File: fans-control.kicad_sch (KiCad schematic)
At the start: 53 parts, among them J2 PinHeader_1x4_P2.5mm_Drill1mm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, J3 PinHeader_1x4_P2.5mm_Drill1mm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, J4 PinHeader_1x4_P2.5mm_Drill1mm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, J5 PinHeader_1x4_P2.5mm_Drill1mm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, Q4 2N7002K-T1-E3, Q5 BSS138PW, U5 LM339_TSSOP_Split, U6 TS5A3359_VSSOP, U7 74CBTLV3257_VQFN, U8 74VHC153FT

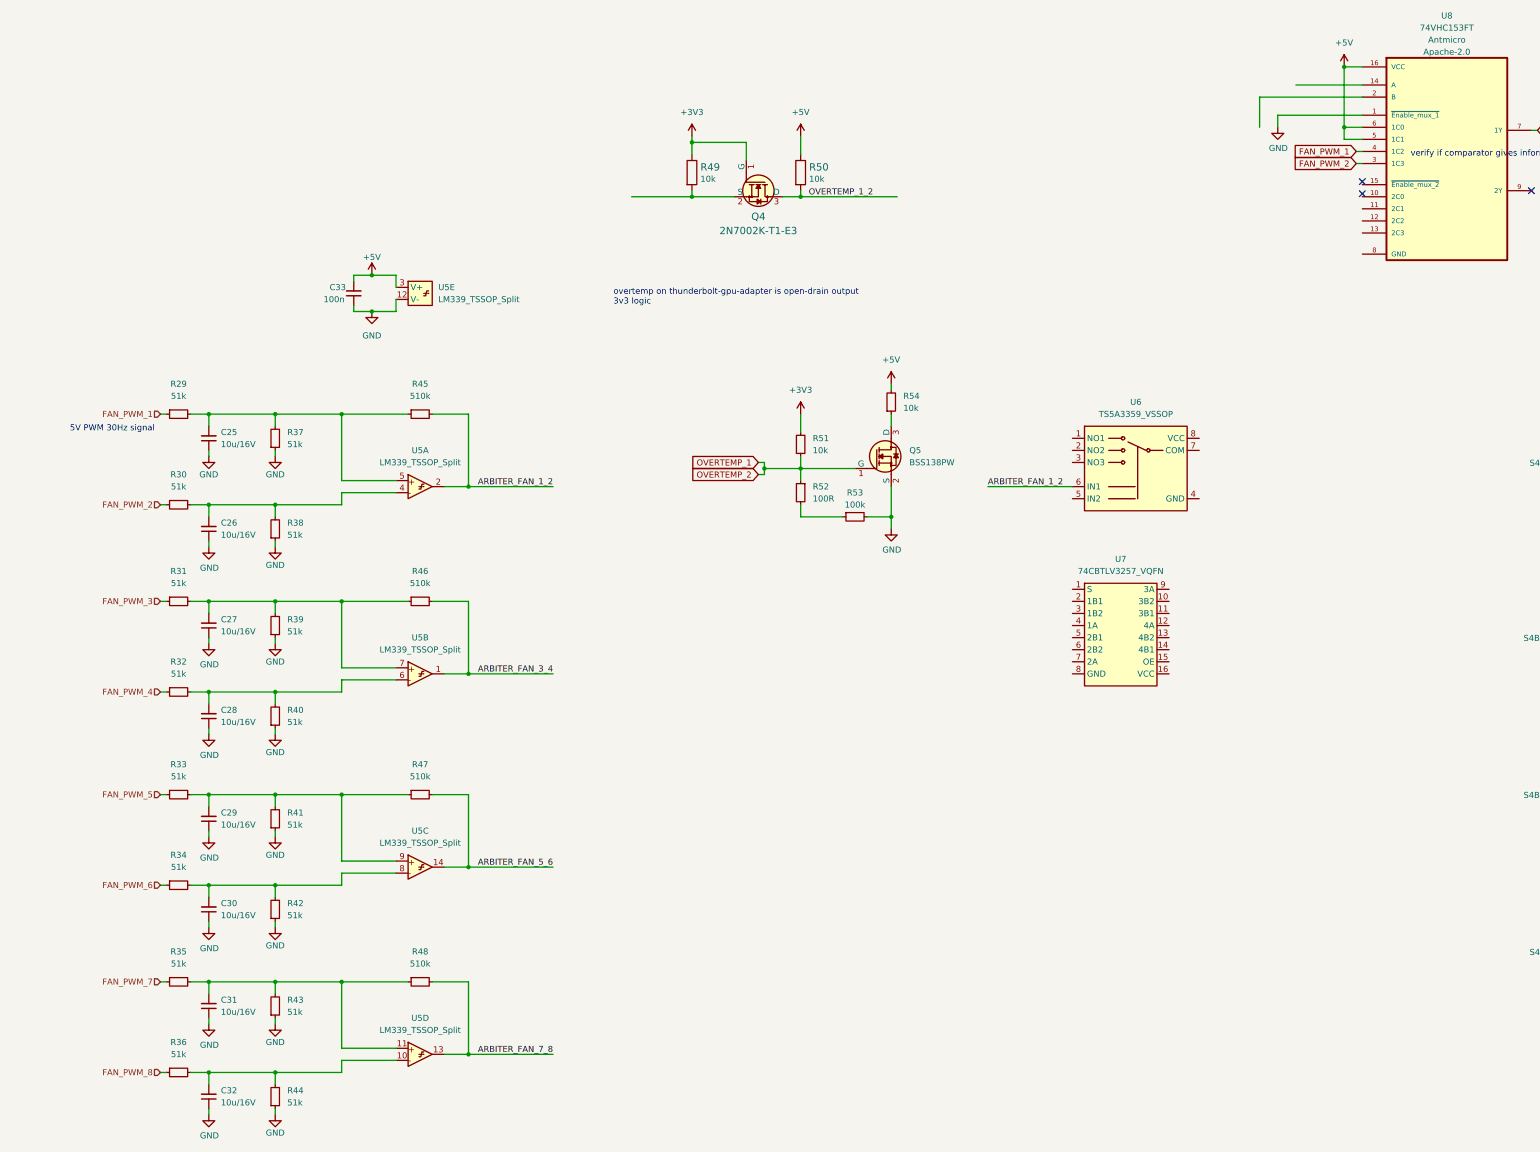
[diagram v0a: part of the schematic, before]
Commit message: Add mux for temp signals
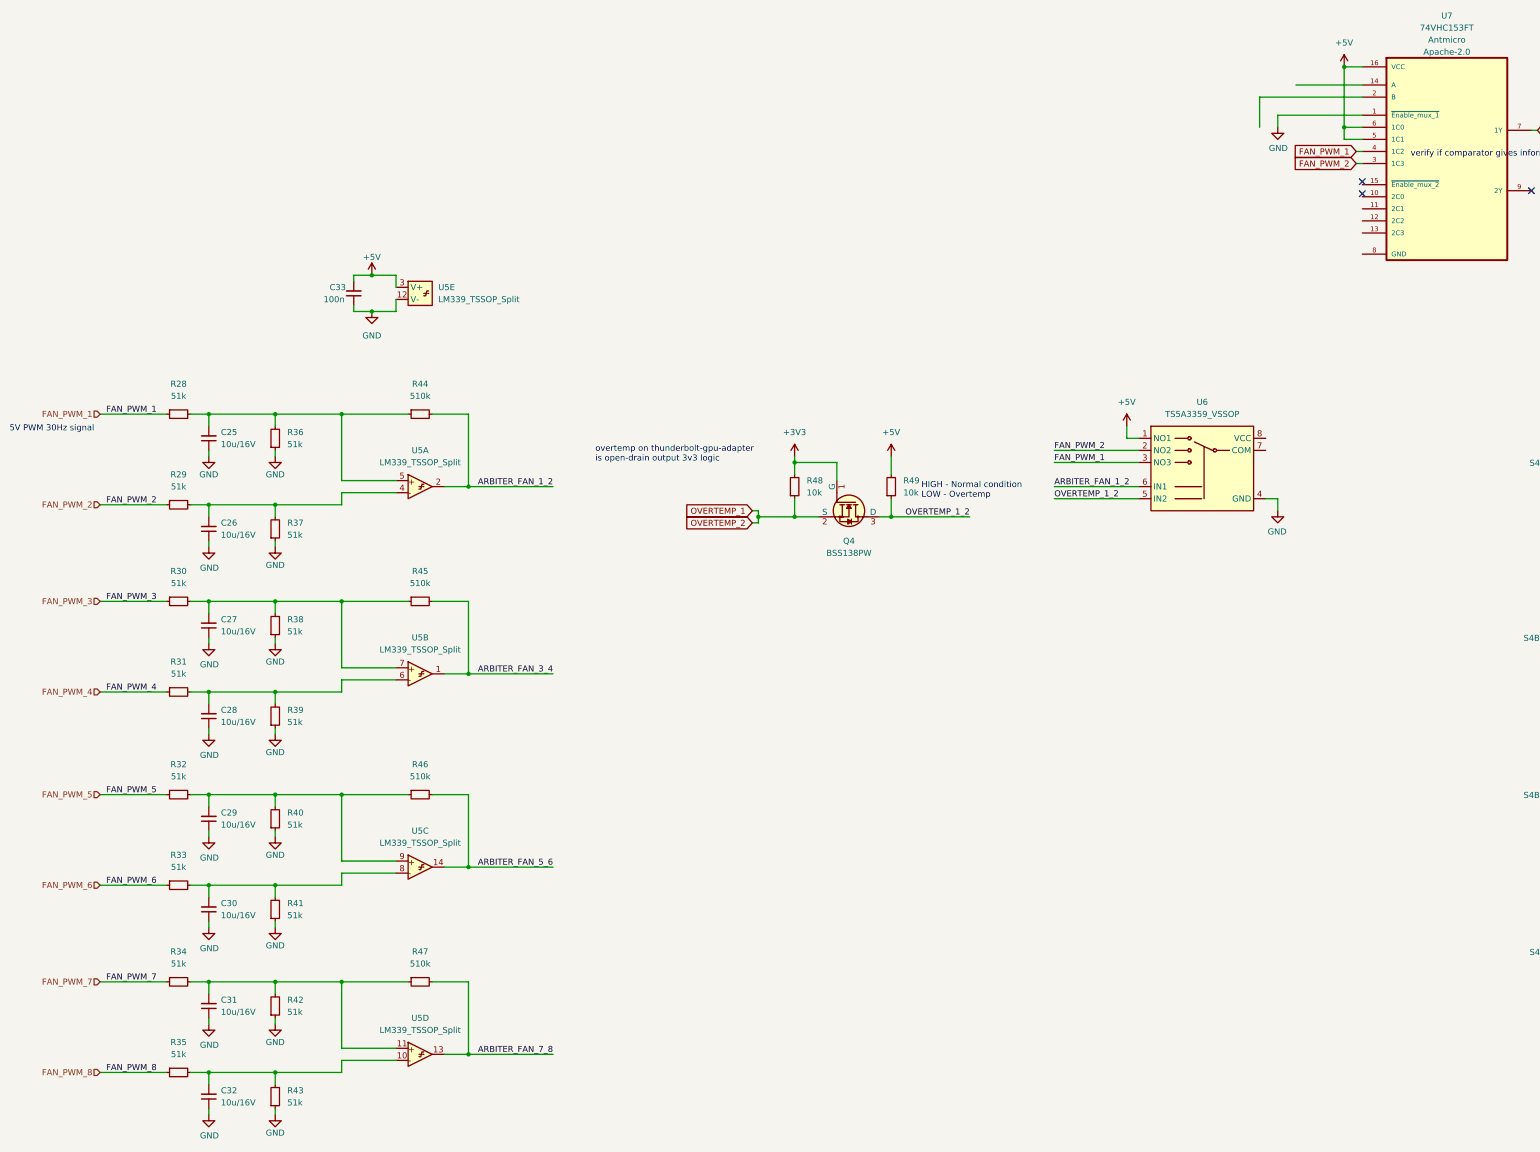
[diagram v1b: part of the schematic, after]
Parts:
- removed Q4: 2N7002K-T1-E3, antmicro-footprints:SOT-23-3, symbol antmicroTransistorsFETsMOSFETsSingle:2N7002K-T1-E3
- removed Q5: BSS138PW, antmicro-footprints:SC70-3, symbol antmicroTransistorsFETsMOSFETsSingle:BSS138PW
- removed R50, R51, R54: R_10k_0402, antmicro-footprints:R_0402_1005Metric, symbol antmicroResistors0402:R_10k_0402
- removed R52: R_100R_0402, antmicro-footprints:R_0402_1005Metric, symbol antmicroResistors0402:R_100R_0402
- removed R53: R_100k_0402, antmicro-footprints:R_0402_1005Metric, symbol antmicroResistors0402:R_100k_0402
- removed U7: 74CBTLV3257_VQFN, antmicro-footprints:DHVQFN-16-1EP_2.5x3.5mm_P0.5mm, symbol antmicroInterfaceAnalogSwitchesMultiplexersDemultiplexers:74CBTLV3257_VQFN
- added Q4: BSS138PW, antmicro-footprints:SC70-3, symbol antmicroTransistorsFETsMOSFETsSingle:BSS138PW
- added R48: R_10k_0402, antmicro-footprints:R_0402_1005Metric, symbol antmicroResistors0402:R_10k_0402
- R49: Author (none) -> Antmicro; License (none) -> Apache-2.0; MPN CRCW040210K0FKEDHP -> CR0402-FX-1002GLF; Manufacturer VISHAY -> Bourns; Tolerance (none) -> 1%
- renumbered R29 to R28, R30 to R29, R31 to R30, R32 to R31, R33 to R32, R34 to R33, R35 to R34, R36 to R35, R37 to R36, R38 to R37, R39 to R38, R40 to R39, R41 to R40, R42 to R41, R43 to R42, R44 to R43, R45 to R44, R46 to R45, R47 to R46, R48 to R47, U8 to U7
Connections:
- net +3V3: now also Q4.1 (G), R48.2; no longer R49.1
- net +5V: now also R49.2, U6.1 (NO1)
- net FAN_PWM_1: now also U6.3 (NO3)
- net FAN_PWM_2: now also U6.2 (NO2)
- net GND: now also U6.4 (GND)
- net OVERTEMP_1: now also Q4.2 (S), R48.1
- net OVERTEMP_1_2: now also R49.1, U6.5 (IN2), Q4.3 (D)
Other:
- note added: "HIGH - Normal condition LOW - Overtemp"
- moved on the sheet: U6

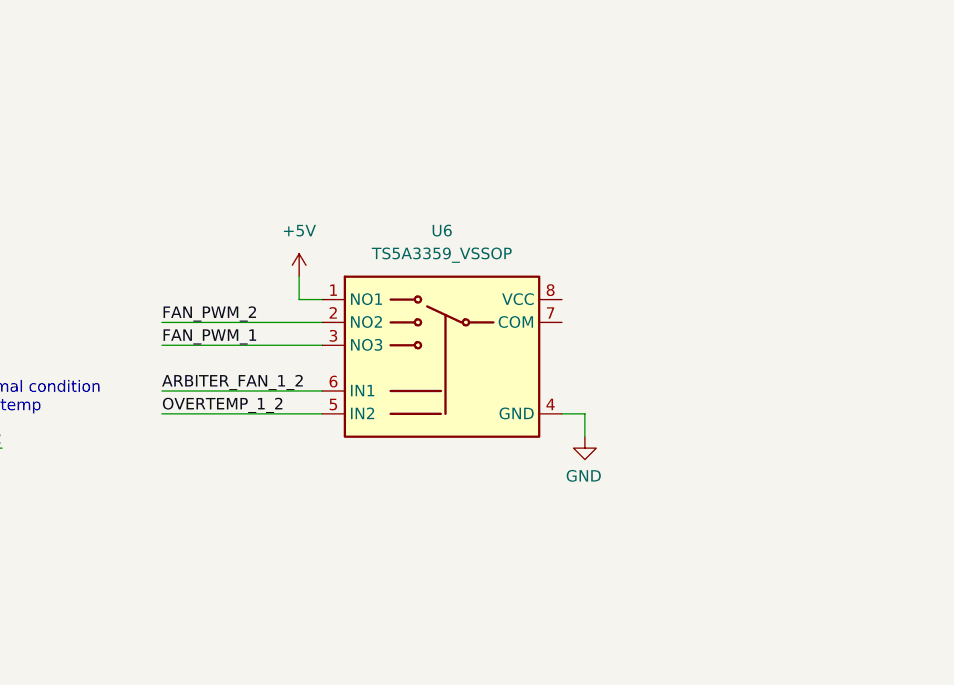
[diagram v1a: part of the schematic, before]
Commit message: Replace ft4232
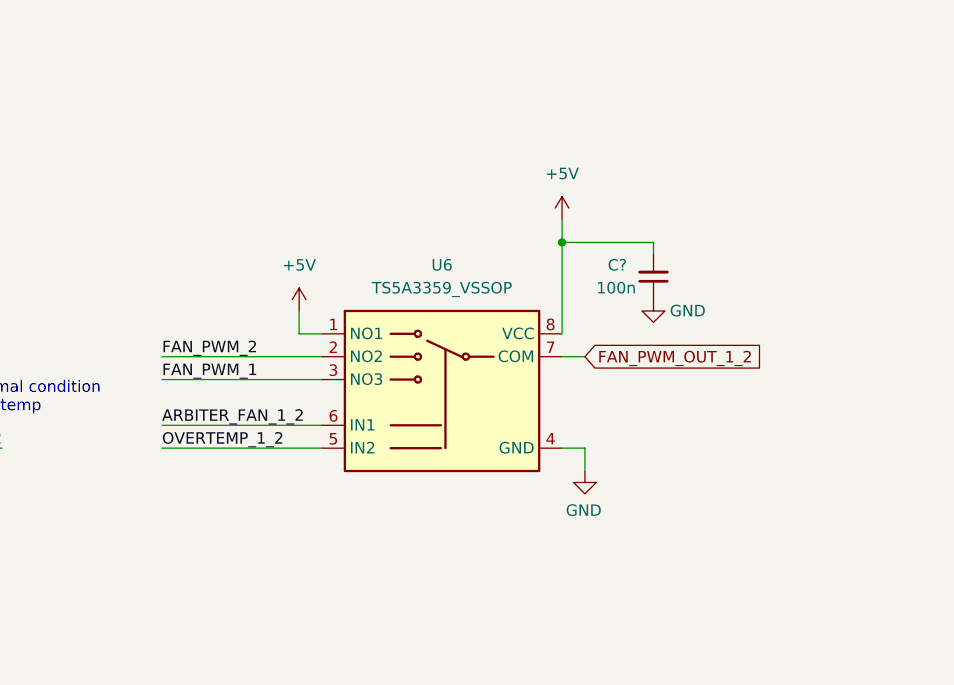
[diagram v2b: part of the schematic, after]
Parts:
- added C?: C_100n_0402, antmicro-footprints:C_0402_1005Metric, symbol antmicroCapacitors0402:C_100n_0402
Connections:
- net +5V: now also U6.8 (VCC), C?.2
- net FAN_PWM_OUT_1_2: now also U6.7 (COM)
- net GND: now also C?.1
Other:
- moved on the sheet: U6

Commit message: Reannotate
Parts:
- gave numbers to parts that had none: 1
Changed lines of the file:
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@@
   (symbol (lib_id "antmicropower:+5V") (at 294.64 -13.335 0) (unit 1)
     (in_bom yes) (on_board yes) (fields_autoplaced)
-    (property "Reference" "#PWR073" (id 0) (at 309.88 -10.795 0)
+    (property "Reference" "#PWR075" (id 0) (at 309.88 -10.795 0)
       (effects (font (size 1.27 1.27) (thickness 0.15)) (justify left bottom) hide)
     )
@@
   (symbol (lib_id "antmicropower:GND") (at 346.71 128.27 0) (unit 1)
     (in_bom yes) (on_board yes)
-    (property "Reference" "#PWR075" (id 0) (at 346.71 134.62 0)
+    (property "Reference" "#PWR077" (id 0) (at 346.71 134.62 0)
       (effects (font (size 1.27 1.27)) hide)
     )
@@
   (symbol (lib_id "antmicropower:GND") (at 288.29 64.77 0) (mirror y) (unit 1)
     (in_bom yes) (on_board yes)
-    (property "Reference" "#PWR?" (id 0) (at 288.29 71.12 0)
+    (property "Reference" "#PWR074" (id 0) (at 288.29 71.12 0)
       (effects (font (size 1.27 1.27)) hide)
     )
@@
   (symbol (lib_id "antmicropower:GND") (at 280.67 -0.635 0) (unit 1)
     (in_bom yes) (on_board yes)
-    (property "Reference" "#PWR071" (id 0) (at 280.67 5.715 0)
+    (property "Reference" "#PWR072" (id 0) (at 280.67 5.715 0)
       (effects (font (size 1.27 1.27)) hide)
     )
@@
   (symbol (lib_id "antmicropower:GND") (at 347.98 194.31 0) (unit 1)
     (in_bom yes) (on_board yes)
-    (property "Reference" "#PWR077" (id 0) (at 347.98 200.66 0)
+    (property "Reference" "#PWR079" (id 0) (at 347.98 200.66 0)
       (effects (font (size 1.27 1.27)) hide)
     )
@@
   (symbol (lib_id "antmicropower:+5V") (at 278.13 55.88 0) (mirror y) (unit 1)
     (in_bom yes) (on_board yes) (fields_autoplaced)
-    (property "Reference" "#PWR?" (id 0) (at 262.89 58.42 0)
+    (property "Reference" "#PWR071" (id 0) (at 262.89 58.42 0)
       (effects (font (size 1.27 1.27) (thickness 0.15)) (justify left bottom) hide)
     )
@@
   (symbol (lib_id "antmicroCapacitors0402:C_100n_0402") (at 288.29 64.77 90) (unit 1)
     (in_bom yes) (on_board yes)
-    (property "Reference" "C?" (id 0) (at 283.21 60.96 90)
+    (property "Reference" "C34" (id 0) (at 283.21 60.96 90)
       (effects (font (size 1.27 1.27) (thickness 0.15)) (justify right))
     )
@@
   (symbol (lib_id "antmicropower:GND") (at 347.98 91.44 0) (unit 1)
     (in_bom yes) (on_board yes)
-    (property "Reference" "#PWR076" (id 0) (at 347.98 97.79 0)
+    (property "Reference" "#PWR078" (id 0) (at 347.98 97.79 0)
       (effects (font (size 1.27 1.27)) hide)
     )
@@
   (symbol (lib_id "antmicropower:GND") (at 345.44 161.29 0) (unit 1)
     (in_bom yes) (on_board yes)
-    (property "Reference" "#PWR074" (id 0) (at 345.44 167.64 0)
+    (property "Reference" "#PWR076" (id 0) (at 345.44 167.64 0)
       (effects (font (size 1.27 1.27)) hide)
     )
@@
   (symbol (lib_id "antmicropower:GND") (at 280.67 83.82 0) (mirror y) (unit 1)
     (in_bom yes) (on_board yes)
-    (property "Reference" "#PWR072" (id 0) (at 280.67 90.17 0)
-      (effects (font (size 1.27 1.27)) hide)
-    )
+    (property "Reference" "#PWR073" (id 0) (at 280.67 90.17 0)
+      (effects (font (size 1.27 1.27)) hide)
+    )

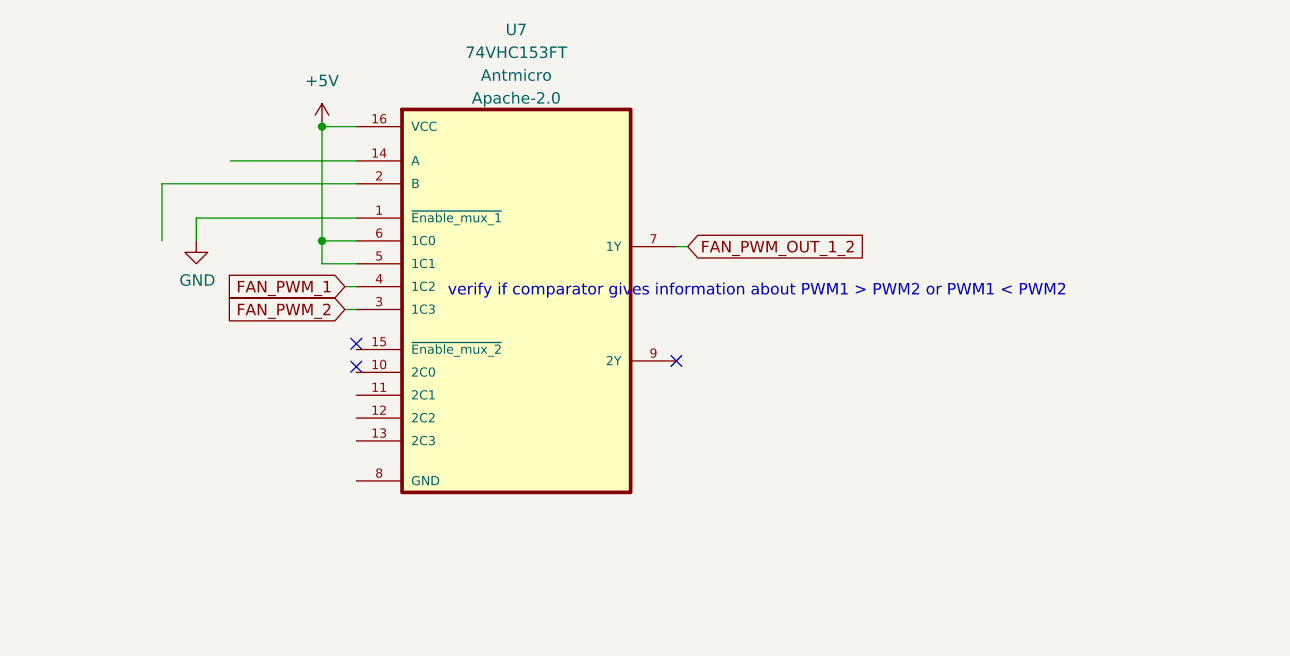
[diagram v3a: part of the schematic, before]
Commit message: Standarize all components and enumerate
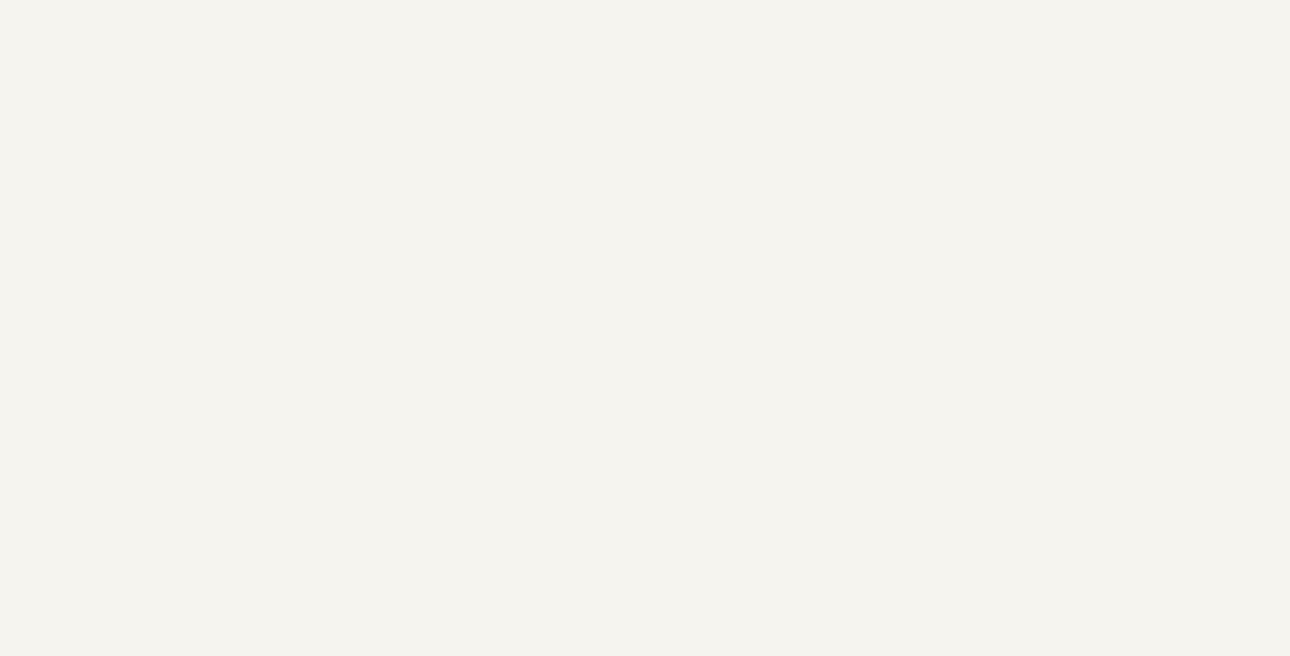
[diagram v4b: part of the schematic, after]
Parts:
- removed U7: 74VHC153FT, antmicro-footprints:TSSOP-16_4.4x5mm_P0.65mm, symbol antmicroInterfaceAnalogSwitchesMultiplexersDemultiplexers:74VHC153FT
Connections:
- no-connect marks 3 -> 0
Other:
- note removed: "verify if comparator gives information about PWM1 > PWM2 or PWM1 < PWM2"
